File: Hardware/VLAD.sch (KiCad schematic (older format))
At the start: 17 parts

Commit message: Added test points everywhere
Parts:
- removed J?: Conn_01x03_Male, symbol Connector:Conn_01x03_Male
- added TP? (x7): TestPoint, symbol Connector:TestPoint
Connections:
- wire segments 79 -> 82
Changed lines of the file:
@@
 EESchema Schematic File Version 4
-LIBS:VLAD-cache
 EELAYER 30 0
 EELAYER END
@@
 	0    1    1    0
 $EndComp
-Text Label 1650 7050 2    50   ~ 0
-SerialTx
-Text Label 1650 6950 2    50   ~ 0
-SerialRx
-Wire Wire Line
-	1750 6950 1650 6950
-Wire Wire Line
-	1750 7050 1650 7050
-$Comp
-L Connector:Conn_01x03_Male J?
-U 1 1 60A45047
-P 1950 7050
-F 0 "J?" H 1922 6982 50  0000 R CNN
-F 1 "Conn_01x03_Male" H 1922 7073 50  0000 R CNN
-F 2 "" H 1950 7050 50  0001 C CNN
-F 3 "~" H 1950 7050 50  0001 C CNN
-	1    1950 7050
-	-1   0    0    1
-$EndComp
-Wire Wire Line
-	1750 7150 1650 7150
-Wire Wire Line
-	1650 7150 1650 7250
-$Comp
-L power:GND #PWR?
-U 1 1 60A47D32
-P 1650 7250
-F 0 "#PWR?" H 1650 7000 50  0001 C CNN
-F 1 "GND" H 1655 7077 50  0000 C CNN
-F 2 "" H 1650 7250 50  0001 C CNN
-F 3 "" H 1650 7250 50  0001 C CNN
-	1    1650 7250
-	1    0    0    -1
-$EndComp
 $Sheet
 S 9850 1050 1000 550
@@
 F1 "PowerCircuitry.sch" 50
 $EndSheet
+$Comp
+L Connector:TestPoint TP?
+U 1 1 607C855A
+P 2500 1500
+F 0 "TP?" V 2454 1688 50  0000 L CNN
+F 1 "TestPoint" V 2545 1688 50  0000 L CNN
+F 2 "" H 2700 1500 50  0001 C CNN
+F 3 "~" H 2700 1500 50  0001 C CNN
+	1    2500 1500
+	0    1    1    0
+$EndComp
+Wire Wire Line
+	2500 1500 2350 1500
+$Comp
+L Connector:TestPoint TP?
+U 1 1 607CA5C6
+P 2500 1900
+F 0 "TP?" V 2454 2088 50  0000 L CNN
+F 1 "TestPoint" V 2545 2088 50  0000 L CNN
+F 2 "" H 2700 1900 50  0001 C CNN
+F 3 "~" H 2700 1900 50  0001 C CNN
+	1    2500 1900
+	0    1    1    0
+$EndComp
+Wire Wire Line
+	2500 1900 2350 1900
+$Comp
+L Connector:TestPoint TP?
+U 1 1 607CC68B
+P 2500 1700
+F 0 "TP?" V 2454 1888 50  0000 L CNN
+F 1 "TestPoint" V 2545 1888 50  0000 L CNN
+F 2 "" H 2700 1700 50  0001 C CNN
+F 3 "~" H 2700 1700 50  0001 C CNN
+	1    2500 1700
+	0    1    1    0
+$EndComp
+Wire Wire Line
+	2500 1700 2350 1700
+Text Label 2350 1500 0    50   ~ 0
+SCLK
+Text Label 2350 1900 0    50   ~ 0
+MISO
+Text Label 2350 1700 0    50   ~ 0
+MOSI
+$Comp
+L Connector:TestPoint TP?
+U 1 1 607DC320
+P 2500 2100
+F 0 "TP?" V 2454 2288 50  0000 L CNN
+F 1 "TestPoint" V 2545 2288 50  0000 L CNN
+F 2 "" H 2700 2100 50  0001 C CNN
+F 3 "~" H 2700 2100 50  0001 C CNN
+	1    2500 2100
+	0    1    1    0
+$EndComp
+Wire Wire Line
+	2500 2100 2350 2100
+$Comp
+L Connector:TestPoint TP?
+U 1 1 607DE57B
+P 2500 2300
+F 0 "TP?" V 2454 2488 50  0000 L CNN
+F 1 "TestPoint" V 2545 2488 50  0000 L CNN
+F 2 "" H 2700 2300 50  0001 C CNN
+F 3 "~" H 2700 2300 50  0001 C CNN
+	1    2500 2300
+	0    1    1    0
+$EndComp
+Wire Wire Line
+	2500 2300 2350 2300
+Text Label 2350 2100 0    50   ~ 0
+RadioCS
+Text Label 2350 2300 0    50   ~ 0
+SDCS
+$Comp
+L Connector:TestPoint TP?
+U 1 1 607E4763
+P 1900 7050
+F 0 "TP?" V 1854 7238 50  0000 L CNN
+F 1 "TestPoint" V 1945 7238 50  0000 L CNN
+F 2 "" H 2100 7050 50  0001 C CNN
+F 3 "~" H 2100 7050 50  0001 C CNN
+	1    1900 7050
+	0    1    1    0
+$EndComp
+Wire Wire Line
+	1900 7050 1750 7050
+$Comp
+L Connector:TestPoint TP?
+U 1 1 607E6D53
+P 1900 7250
+F 0 "TP?" V 1854 7438 50  0000 L CNN
+F 1 "TestPoint" V 1945 7438 50  0000 L CNN
+F 2 "" H 2100 7250 50  0001 C CNN
+F 3 "~" H 2100 7250 50  0001 C CNN
+	1    1900 7250
+	0    1    1    0
+$EndComp
+Wire Wire Line
+	1900 7250 1750 7250
+Text Label 1750 7050 0    50   ~ 0
+EN
+Text Label 1750 7250 0    50   ~ 0
+IO0
 $EndSCHEMATC

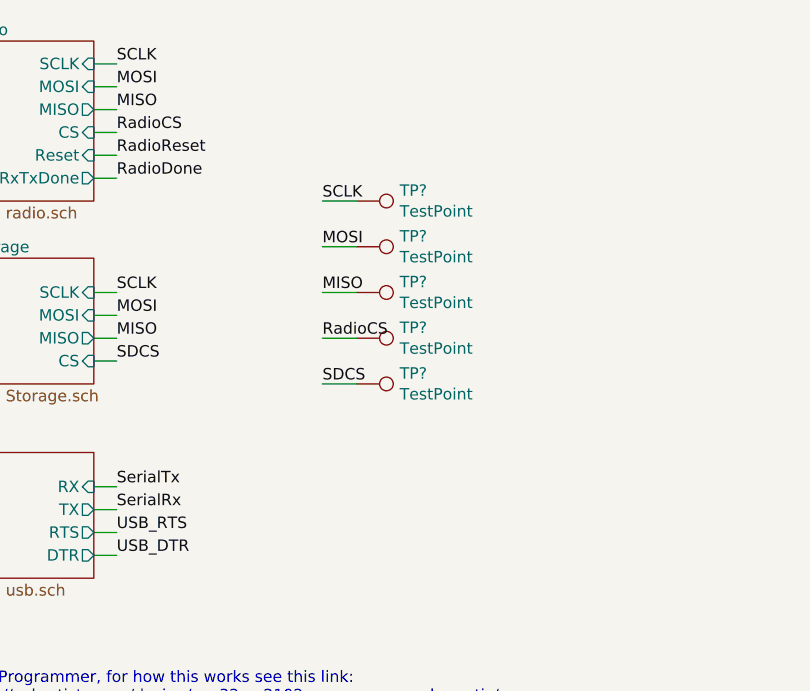
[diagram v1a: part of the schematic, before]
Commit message: Added pull-ups to CS pins
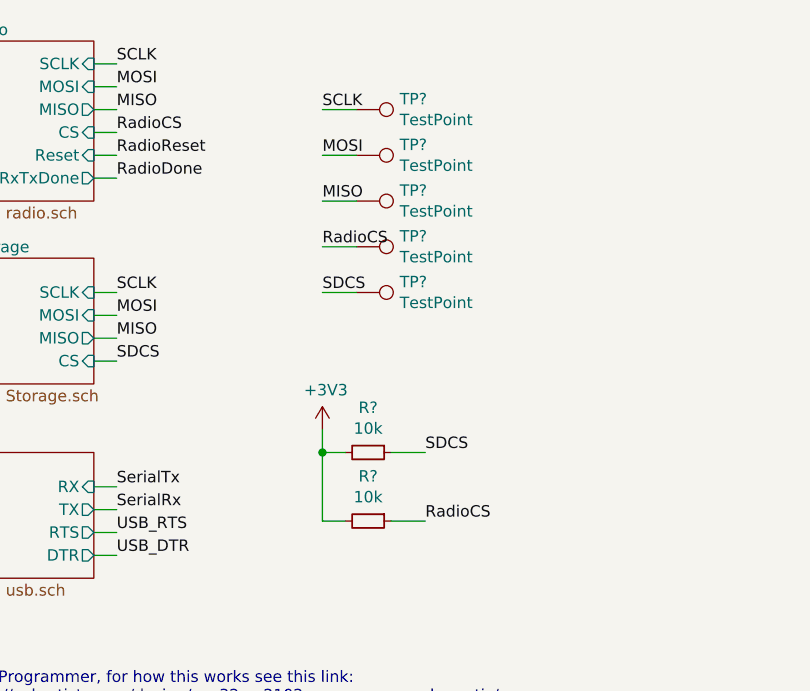
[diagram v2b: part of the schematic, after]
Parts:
- added R? (x2): 10k, symbol Device:R_Small
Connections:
- net +3V3: now also R?.2, R?.2
- net RadioCS: now also R?.1
- net SDCS: now also R?.1
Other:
- moved on the sheet: TP?
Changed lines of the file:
@@
 L Connector:TestPoint TP?
 U 1 1 607C855A
+P 2500 1100
+F 0 "TP?" V 2454 1288 50  0000 L CNN
+F 1 "TestPoint" V 2545 1288 50  0000 L CNN
+F 2 "" H 2700 1100 50  0001 C CNN
+F 3 "~" H 2700 1100 50  0001 C CNN
+	1    2500 1100
+	0    1    1    0
+$EndComp
+Wire Wire Line
+	2500 1100 2350 1100
+$Comp
+L Connector:TestPoint TP?
+U 1 1 607CA5C6
 P 2500 1500
 F 0 "TP?" V 2454 1688 50  0000 L CNN
@@
 $Comp
 L Connector:TestPoint TP?
-U 1 1 607CA5C6
+U 1 1 607CC68B
+P 2500 1300
+F 0 "TP?" V 2454 1488 50  0000 L CNN
+F 1 "TestPoint" V 2545 1488 50  0000 L CNN
+F 2 "" H 2700 1300 50  0001 C CNN
+F 3 "~" H 2700 1300 50  0001 C CNN
+	1    2500 1300
+	0    1    1    0
+$EndComp
+Wire Wire Line
+	2500 1300 2350 1300
+Text Label 2350 1100 0    50   ~ 0
+SCLK
+Text Label 2350 1500 0    50   ~ 0
+MISO
+Text Label 2350 1300 0    50   ~ 0
+MOSI
+$Comp
+L Connector:TestPoint TP?
+U 1 1 607DC320
+P 2500 1700
+F 0 "TP?" V 2454 1888 50  0000 L CNN
+F 1 "TestPoint" V 2545 1888 50  0000 L CNN
+F 2 "" H 2700 1700 50  0001 C CNN
+F 3 "~" H 2700 1700 50  0001 C CNN
+	1    2500 1700
+	0    1    1    0
+$EndComp
+Wire Wire Line
+	2500 1700 2350 1700
+$Comp
+L Connector:TestPoint TP?
+U 1 1 607DE57B
 P 2500 1900
 F 0 "TP?" V 2454 2088 50  0000 L CNN
@@
 Wire Wire Line
 	2500 1900 2350 1900
-$Comp
-L Connector:TestPoint TP?
-U 1 1 607CC68B
-P 2500 1700
-F 0 "TP?" V 2454 1888 50  0000 L CNN
-F 1 "TestPoint" V 2545 1888 50  0000 L CNN
-F 2 "" H 2700 1700 50  0001 C CNN
-F 3 "~" H 2700 1700 50  0001 C CNN
-	1    2500 1700
-	0    1    1    0
-$EndComp
-Wire Wire Line
-	2500 1700 2350 1700
-Text Label 2350 1500 0    50   ~ 0
-SCLK
+Text Label 2350 1700 0    50   ~ 0
+RadioCS
 Text Label 2350 1900 0    50   ~ 0
-MISO
-Text Label 2350 1700 0    50   ~ 0
-MOSI
-$Comp
-L Connector:TestPoint TP?
-U 1 1 607DC320
-P 2500 2100
-F 0 "TP?" V 2454 2288 50  0000 L CNN
-F 1 "TestPoint" V 2545 2288 50  0000 L CNN
-F 2 "" H 2700 2100 50  0001 C CNN
-F 3 "~" H 2700 2100 50  0001 C CNN
-	1    2500 2100
-	0    1    1    0
-$EndComp
-Wire Wire Line
-	2500 2100 2350 2100
-$Comp
-L Connector:TestPoint TP?
-U 1 1 607DE57B
-P 2500 2300
-F 0 "TP?" V 2454 2488 50  0000 L CNN
-F 1 "TestPoint" V 2545 2488 50  0000 L CNN
-F 2 "" H 2700 2300 50  0001 C CNN
-F 3 "~" H 2700 2300 50  0001 C CNN
-	1    2500 2300
-	0    1    1    0
-$EndComp
-Wire Wire Line
-	2500 2300 2350 2300
-Text Label 2350 2100 0    50   ~ 0
-RadioCS
-Text Label 2350 2300 0    50   ~ 0
 SDCS
 $Comp
@@
 Text Label 1750 7250 0    50   ~ 0
 IO0
+$Comp
+L power:+3V3 #PWR?
+U 1 1 607EC630
+P 2350 2500
+F 0 "#PWR?" H 2350 2350 50  0001 C CNN
+F 1 "+3V3" H 2365 2673 50  0000 C CNN
+F 2 "" H 2350 2500 50  0001 C CNN
+F 3 "" H 2350 2500 50  0001 C CNN
+	1    2350 2500
+	1    0    0    -1
+$EndComp
+Wire Wire Line
+	2350 2500 2350 2600
+Wire Wire Line
+	2350 2600 2450 2600
+$Comp
+L Device:R_Small R?
+U 1 1 607EF2CF
+P 2550 2600
+F 0 "R?" V 2354 2600 50  0000 C CNN
+F 1 "10k" V 2445 2600 50  0000 C CNN
+F 2 "" H 2550 2600 50  0001 C CNN
+F 3 "~" H 2550 2600 50  0001 C CNN
+	1    2550 2600
+	0    1    1    0
+$EndComp
+Connection ~ 2350 2600
+Wire Wire Line
+	2350 2900 2450 2900
+Wire Wire Line
+	2350 2600 2350 2900
+Wire Wire Line
+	2650 2600 2800 2600
+Wire Wire Line
+	2650 2900 2800 2900
+Text Label 2800 2600 0    50   ~ 0
+SDCS
+Text Label 2800 2900 0    50   ~ 0
+RadioCS
+$Comp
+L Device:R_Small R?
+U 1 1 608060BD
+P 2550 2900
+F 0 "R?" V 2354 2900 50  0000 C CNN
+F 1 "10k" V 2445 2900 50  0000 C CNN
+F 2 "" H 2550 2900 50  0001 C CNN
+F 3 "~" H 2550 2900 50  0001 C CNN
+	1    2550 2900
+	0    1    1    0
+$EndComp
 $EndSCHEMATC

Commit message: Added Buzzer
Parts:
- added BZ?: Buzzer, symbol Device:Buzzer
- added R?: R_Small, symbol Device:R_Small
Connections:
- net GND: now also BZ?.2 (+)
- net Buzzer: now reaches U?.10 (IO25)
- net Buzzer: now also R?.2
- new net: BZ?.1 (-), R?.1
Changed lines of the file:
@@
 	0    1    1    0
 $EndComp
+$Comp
+L Device:Buzzer BZ?
+U 1 1 607EA96B
+P 9050 5050
+F 0 "BZ?" V 9101 4863 50  0000 R CNN
+F 1 "Buzzer" V 9010 4863 50  0000 R CNN
+F 2 "" V 9025 5150 50  0001 C CNN
+F 3 "~" V 9025 5150 50  0001 C CNN
+	1    9050 5050
+	0    -1   -1   0
+$EndComp
+Wire Wire Line
+	9150 5150 9150 5250
+Wire Wire Line
+	8950 5150 8950 5200
+Wire Wire Line
+	8950 5200 8800 5200
+$Comp
+L Device:R_Small R?
+U 1 1 607F07A9
+P 8700 5200
+F 0 "R?" V 8504 5200 50  0000 C CNN
+F 1 "R_Small" V 8595 5200 50  0000 C CNN
+F 2 "" H 8700 5200 50  0001 C CNN
+F 3 "~" H 8700 5200 50  0001 C CNN
+	1    8700 5200
+	0    1    1    0
+$EndComp
+Wire Wire Line
+	8600 5200 8300 5200
+$Comp
+L power:GND #PWR?
+U 1 1 607F3B2D
+P 9150 5250
+F 0 "#PWR?" H 9150 5000 50  0001 C CNN
+F 1 "GND" H 9155 5077 50  0000 C CNN
+F 2 "" H 9150 5250 50  0001 C CNN
+F 3 "" H 9150 5250 50  0001 C CNN
+	1    9150 5250
+	1    0    0    -1
+$EndComp
+Text Label 8300 5200 0    50   ~ 0
+Buzzer
+Wire Wire Line
+	6750 4250 7000 4250
+Text Label 7000 4250 0    50   ~ 0
+Buzzer
 $EndSCHEMATC

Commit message: Added temporary sensor connections
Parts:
- added J?: BMP388, symbol Connector:Conn_01x08_Female
- added J?: BNO055, symbol Connector:Conn_01x06_Female
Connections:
- net +3V3: now also J?.2 (Pin_2), J?.2 (Pin_2)
- net GND: now also J?.3 (Pin_3), J?.3 (Pin_3)
- net SDA: now reaches U?.11 (IO26)
- net SDA: now also J?.4 (Pin_4), J?.5 (Pin_5)
- net SCL: now reaches U?.12 (IO27)
- net SCL: now also J?.4 (Pin_4), J?.5 (Pin_5)
- no-connect marks 6 -> 12
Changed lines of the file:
@@
 Text Label 7000 4250 0    50   ~ 0
 Buzzer
+Wire Wire Line
+	6750 4350 7000 4350
+Wire Wire Line
+	6750 4450 7000 4450
+Text Label 7000 4350 0    50   ~ 0
+SDA
+Text Label 7000 4450 0    50   ~ 0
+SCL
+$Comp
+L Connector:Conn_01x06_Female J?
+U 1 1 60803066
+P 9350 3400
+F 0 "J?" H 9378 3376 50  0000 L CNN
+F 1 "BNO055" H 9378 3285 50  0000 L CNN
+F 2 "" H 9350 3400 50  0001 C CNN
+F 3 "~" H 9350 3400 50  0001 C CNN
+	1    9350 3400
+	1    0    0    -1
+$EndComp
+NoConn ~ 9150 2750
+NoConn ~ 9150 2850
+NoConn ~ 9150 2150
+NoConn ~ 9150 2650
+Text Label 9050 2550 0    50   ~ 0
+SDA
+Text Label 9050 2450 0    50   ~ 0
+SCL
+Wire Wire Line
+	9150 2550 9050 2550
+Wire Wire Line
+	9150 2450 9050 2450
+Wire Wire Line
+	8750 2350 9150 2350
+$Comp
+L power:GND #PWR?
+U 1 1 6080ACCC
+P 8750 2450
+F 0 "#PWR?" H 8750 2200 50  0001 C CNN
+F 1 "GND" H 8755 2277 50  0000 C CNN
+F 2 "" H 8750 2450 50  0001 C CNN
+F 3 "" H 8750 2450 50  0001 C CNN
+	1    8750 2450
+	1    0    0    -1
+$EndComp
+Wire Wire Line
+	8750 2350 8750 2450
+$Comp
+L power:+3V3 #PWR?
+U 1 1 60806D9C
+P 9050 2150
+F 0 "#PWR?" H 9050 2000 50  0001 C CNN
+F 1 "+3V3" H 9065 2323 50  0000 C CNN
+F 2 "" H 9050 2150 50  0001 C CNN
+F 3 "" H 9050 2150 50  0001 C CNN
+	1    9050 2150
+	1    0    0    -1
+$EndComp
+Wire Wire Line
+	9050 2250 9050 2150
+Wire Wire Line
+	9150 2250 9050 2250
+$Comp
+L Connector:Conn_01x08_Female J?
+U 1 1 607FE864
+P 9350 2450
+F 0 "J?" H 9378 2426 50  0000 L CNN
+F 1 "BMP388" H 9378 2335 50  0000 L CNN
+F 2 "" H 9350 2450 50  0001 C CNN
+F 3 "~" H 9350 2450 50  0001 C CNN
+	1    9350 2450
+	1    0    0    -1
+$EndComp
+Text Label 9050 3500 0    50   ~ 0
+SDA
+Wire Wire Line
+	9150 3600 9050 3600
+Wire Wire Line
+	9150 3500 9050 3500
+Wire Wire Line
+	8750 3400 9150 3400
+$Comp
+L power:GND #PWR?
+U 1 1 60834281
+P 8750 3500
+F 0 "#PWR?" H 8750 3250 50  0001 C CNN
+F 1 "GND" H 8755 3327 50  0000 C CNN
+F 2 "" H 8750 3500 50  0001 C CNN
+F 3 "" H 8750 3500 50  0001 C CNN
+	1    8750 3500
+	1    0    0    -1
+$EndComp
+Wire Wire Line
+	8750 3400 8750 3500
+$Comp
+L power:+3V3 #PWR?
+U 1 1 60834288
+P 9050 3200
+F 0 "#PWR?" H 9050 3050 50  0001 C CNN
+F 1 "+3V3" H 9065 3373 50  0000 C CNN
+F 2 "" H 9050 3200 50  0001 C CNN
+F 3 "" H 9050 3200 50  0001 C CNN
+	1    9050 3200
+	1    0    0    -1
+$EndComp
+Wire Wire Line
+	9050 3300 9050 3200
+Wire Wire Line
+	9150 3300 9050 3300
+NoConn ~ 9150 3200
+NoConn ~ 9150 3700
+Text Label 9050 3600 0    50   ~ 0
+SCL
 $EndSCHEMATC

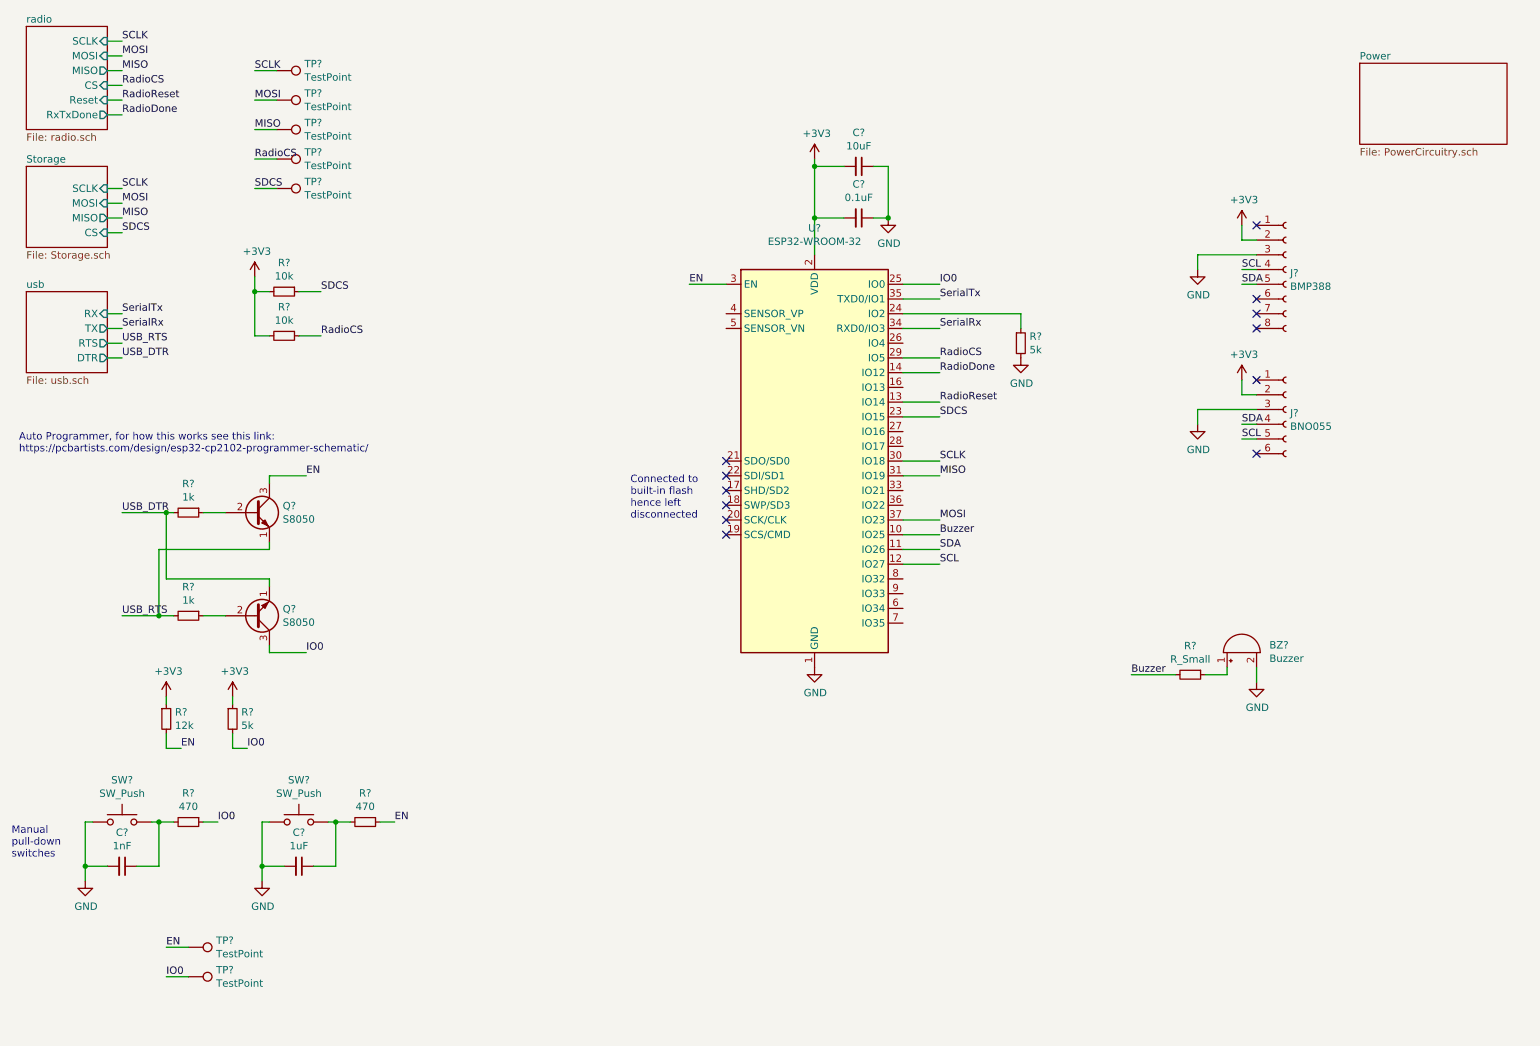
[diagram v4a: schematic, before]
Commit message: Fixed some of the ERC errors
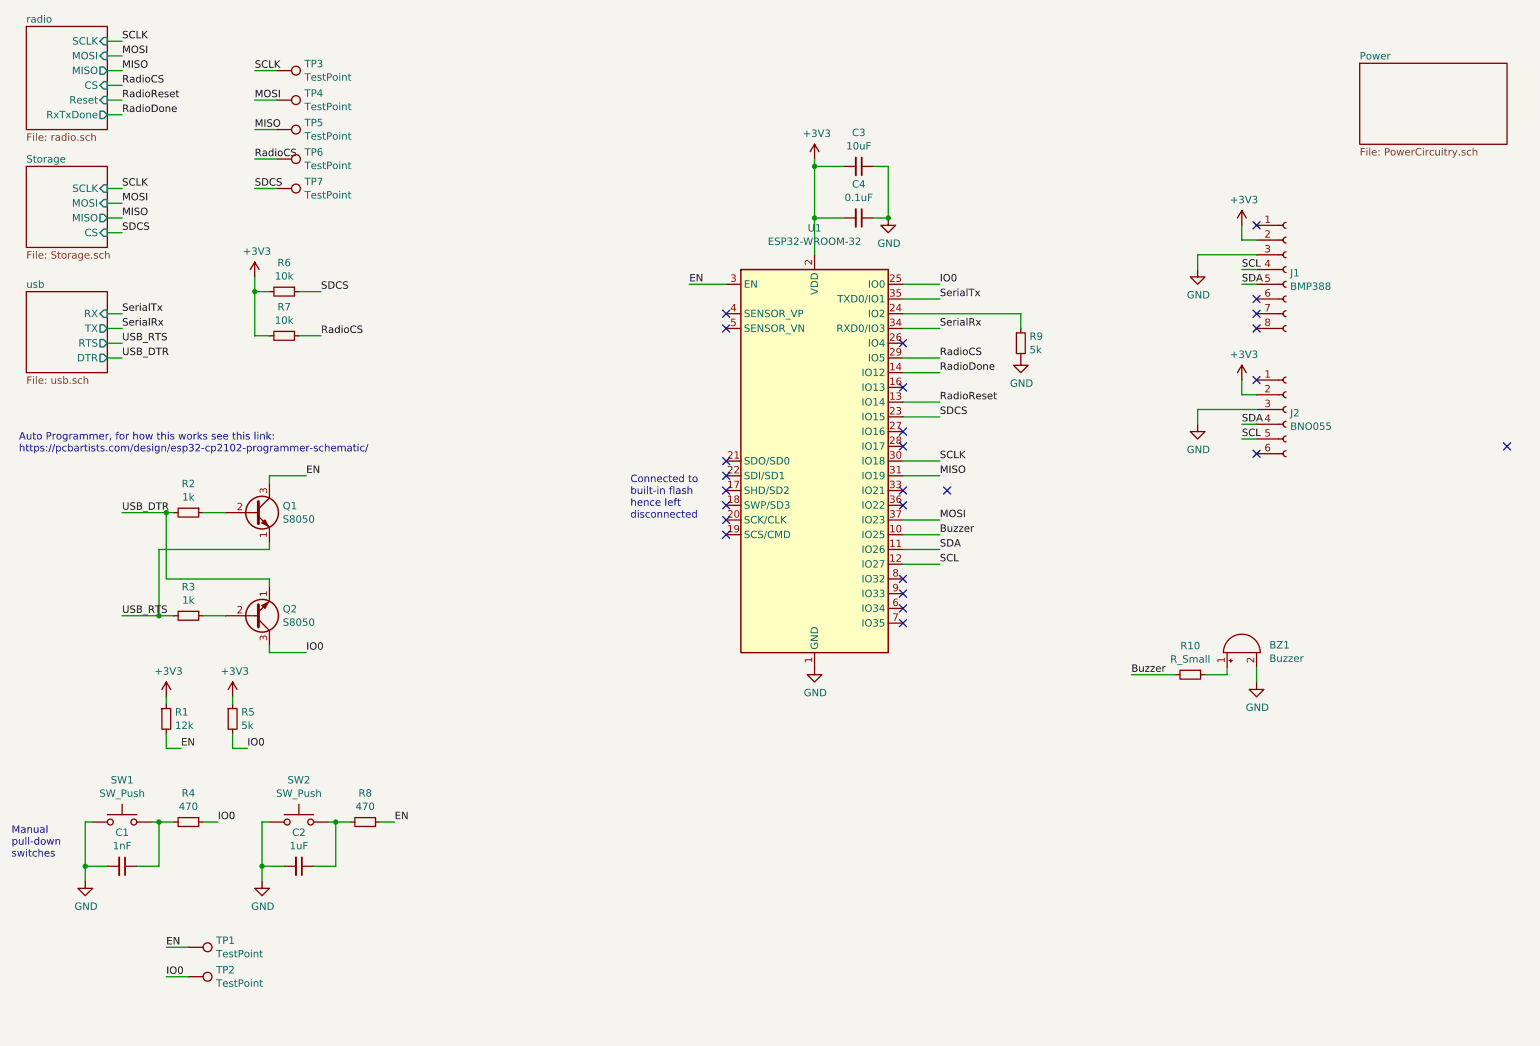
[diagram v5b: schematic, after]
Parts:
- gave numbers to parts that had none: 29
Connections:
- no-connect marks 12 -> 26
